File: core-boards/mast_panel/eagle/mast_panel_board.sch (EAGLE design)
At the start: 30 parts, among them J1 2-PIN_2MM-V, J4 4-PIN_2MM-H, U1 ATMEGA328P-AUR, U3 MCP2551T-I/SN

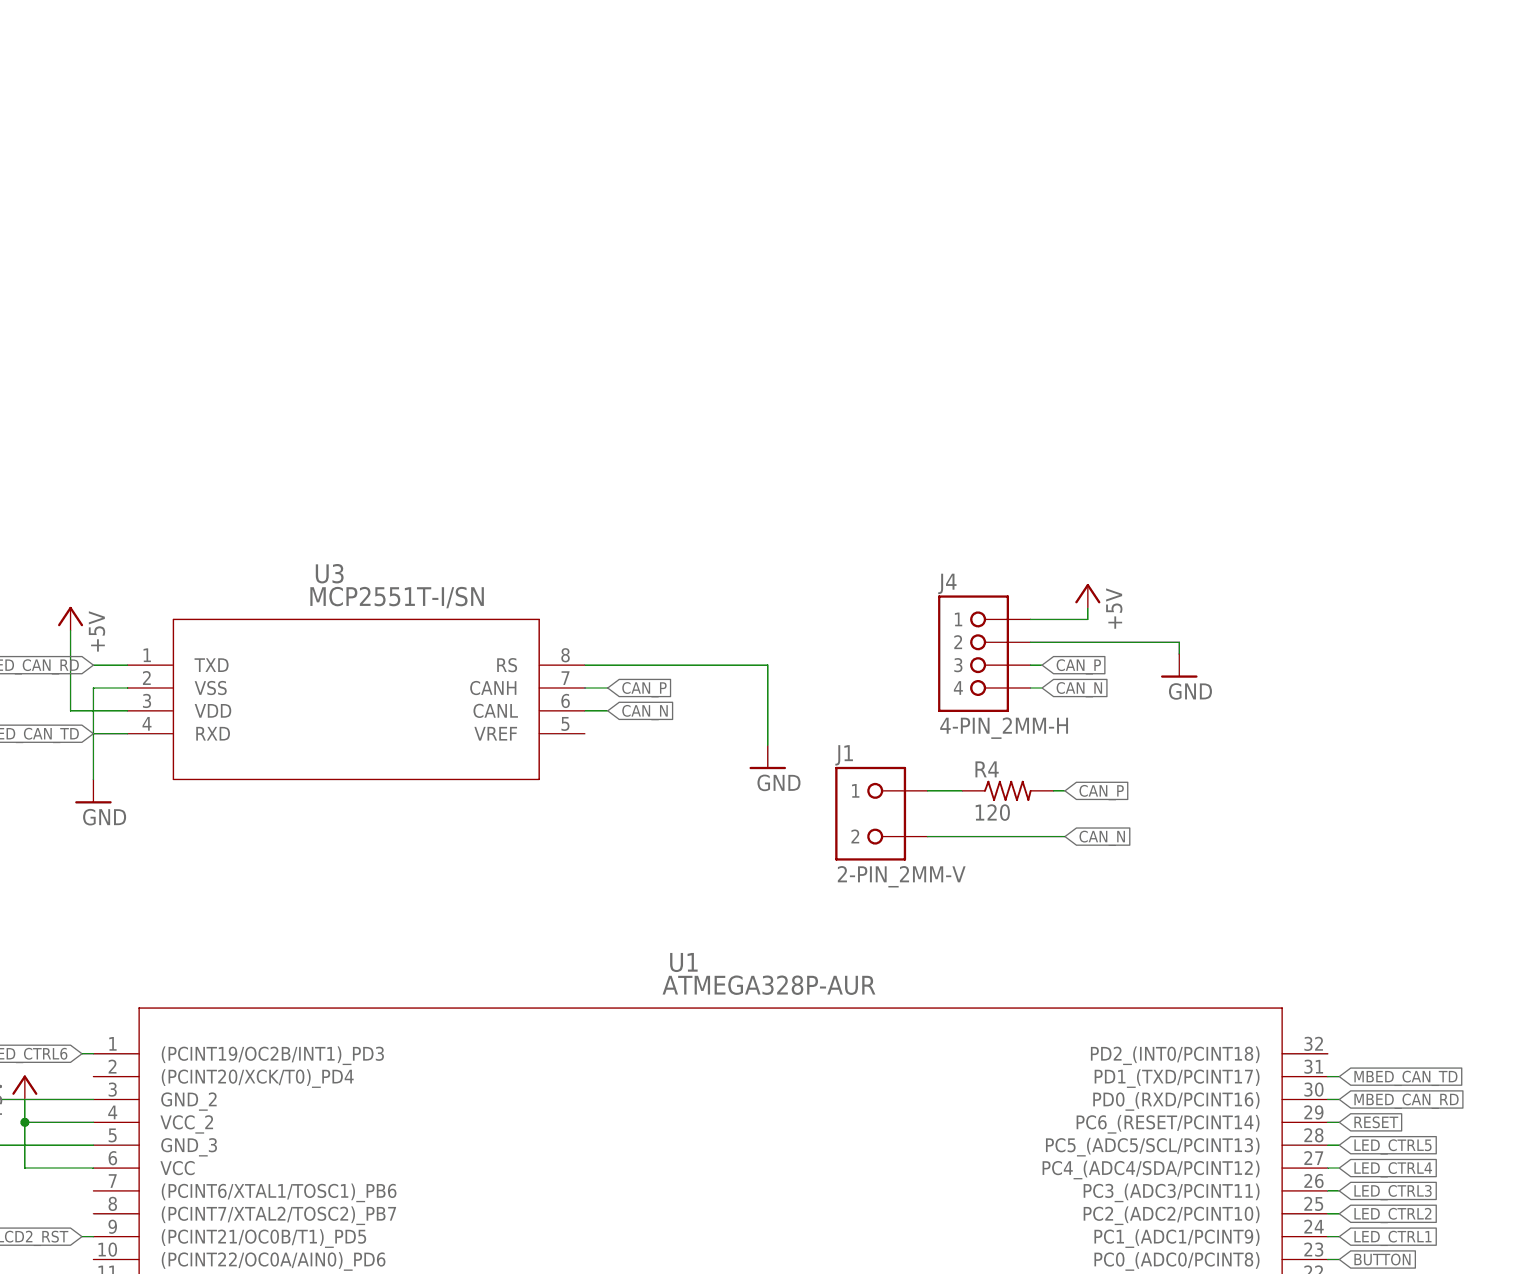
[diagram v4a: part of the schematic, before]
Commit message: CAN Addition
Added the new CAN Controller. Routing on the board still needs to be done.
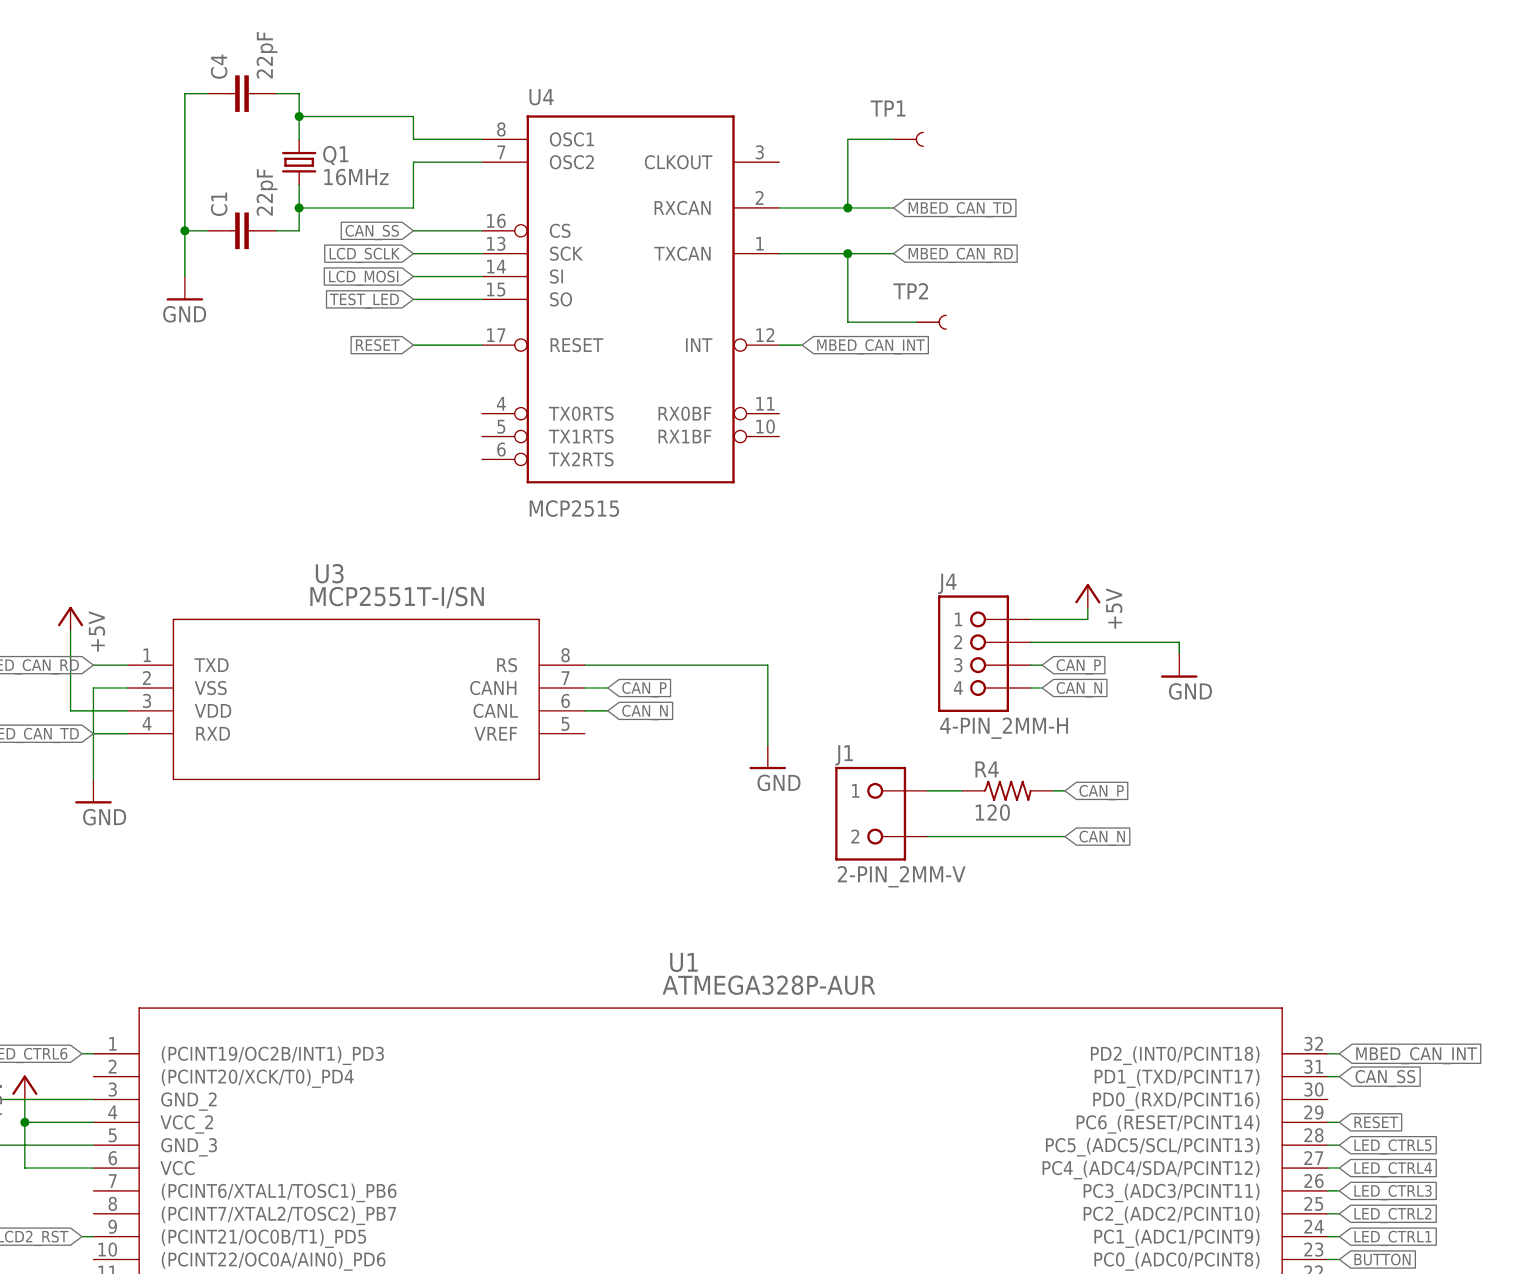
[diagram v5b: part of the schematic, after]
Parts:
- added C1, C4: 22pF, SparkFun-Capacitors:22PF-50V-5%(0603)
- added Q1: 16MHz, SparkFun-FreqCtrl:CRYSTAL5X3
- added TP1, TP2: TEST-POINT3X5, SparkFun-Passives:TEST-POINT3X5
- added U4: MCP2515, SparkFun-DigitalIC:MCP2510SO
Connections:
- new net CAN_SS: U1.PD1_(TXD/PCINT17), U4>NAME.CS
- new net MBED_CAN_INT: U1.PD2_(INT0/PCINT18), U4>NAME.INT
- new net N$17: C4.2, Q1.2, U4>NAME.OSC1
- new net N$18: C1.2, Q1.1, U4>NAME.OSC2
- net GND: now also C1.1, C4.1
- net LCD_MOSI: now also U4>NAME.SI
- net LCD_SCLK: now also U4>NAME.SCK
- net MBED_CAN_RD: now also TP2.1, U4>NAME.TXCAN; no longer U1.PD0_(RXD/PCINT16)
- net MBED_CAN_TD: now also TP1.1, U4>NAME.RXCAN; no longer U1.PD1_(TXD/PCINT17)
- net RESET: now also U4>NAME.RESET
- net TEST_LED: now also U4>NAME.SO
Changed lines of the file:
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@@
 <part name="R9" library="rcl" library_urn="urn:adsk.eagle:library:334" deviceset="R-US_" device="R0805" package3d_urn="urn:adsk.eagle:package:23553/2" value="50kO"/>
 <part name="R10" library="rcl" library_urn="urn:adsk.eagle:library:334" deviceset="R-US_" device="R0805" package3d_urn="urn:adsk.eagle:package:23553/2" value="50kO"/>
+<part name="U4" library="SparkFun-DigitalIC" deviceset="MCP2510" device="SO" value="MCP2515"/>
+<part name="Q1" library="SparkFun-FreqCtrl" deviceset="CRYSTAL" device="5X3" value="16MHz"/>
+<part name="C1" library="SparkFun-Capacitors" deviceset="22PF-50V-5%(0603)" device="" value="22pF"/>
+<part name="C4" library="SparkFun-Capacitors" deviceset="22PF-50V-5%(0603)" device="" value="22pF"/>
+<part name="GND14" library="SparkFun-Aesthetics" deviceset="GND" device=""/>
+<part name="TP1" library="SparkFun-Passives" deviceset="TEST-POINT" device="3X5" value="TEST-POINT3X5"/>
+<part name="TP2" library="SparkFun-Passives" deviceset="TEST-POINT" device="3X5" value="TEST-POINT3X5"/>
 </parts>
 <sheets>
@@
 <attribute name="VALUE" x="-44.45" y="-106.172" size="1.778" layer="96"/>
 </instance>
+<instance part="U4" gate="&gt;NAME" x="78.74" y="88.9" smashed="yes">
+<attribute name="NAME" x="68.58" y="105.41" size="1.778" layer="95"/>
+<attribute name="VALUE" x="68.58" y="59.69" size="1.778" layer="96"/>
+</instance>
+<instance part="Q1" gate="G$1" x="43.18" y="99.06" smashed="yes" rot="R90">
+<attribute name="NAME" x="45.72" y="99.06" size="1.778" layer="95"/>
+<attribute name="VALUE" x="45.72" y="96.52" size="1.778" layer="96"/>
+</instance>
+<instance part="C1" gate="G$1" x="38.1" y="91.44" smashed="yes" rot="R90">
+<attribute name="NAME" x="35.179" y="92.964" size="1.778" layer="95" rot="R90"/>
+<attribute name="VALUE" x="40.259" y="92.964" size="1.778" layer="96" rot="R90"/>
+</instance>
+<instance part="C4" gate="G$1" x="38.1" y="106.68" smashed="yes" rot="R90">
+<attribute name="NAME" x="35.179" y="108.204" size="1.778" layer="95" rot="R90"/>
+<attribute name="VALUE" x="40.259" y="108.204" size="1.778" layer="96" rot="R90"/>
+</instance>
+<instance part="GND14" gate="1" x="30.48" y="83.82" smashed="yes">
+<attribute name="VALUE" x="27.94" y="81.28" size="1.778" layer="96"/>
+</instance>
+<instance part="TP1" gate="G$1" x="109.22" y="101.6" smashed="yes">
+<attribute name="NAME" x="106.68" y="104.14" size="1.778" layer="95"/>
+</instance>
+<instance part="TP2" gate="G$1" x="111.76" y="81.28" smashed="yes">
+<attribute name="NAME" x="109.22" y="83.82" size="1.778" layer="95"/>
+</instance>
 </instances>
 <busses>
@@
 <pinref part="GND13" gate="1" pin="GND"/>
 </segment>
+<segment>
+<wire x1="33.02" y1="106.68" x2="30.48" y2="106.68" width="0.1524" layer="91"/>
+<wire x1="30.48" y1="106.68" x2="30.48" y2="91.44" width="0.1524" layer="91"/>
+<wire x1="30.48" y1="91.44" x2="33.02" y2="91.44" width="0.1524" layer="91"/>
+<wire x1="30.48" y1="86.36" x2="30.48" y2="91.44" width="0.1524" layer="91"/>
+<junction x="30.48" y="91.44"/>
+<pinref part="C4" gate="G$1" pin="1"/>
+<pinref part="C1" gate="G$1" pin="1"/>
+<pinref part="GND14" gate="1" pin="GND"/>
+</segment>
 </net>
 <net name="BUTTON" class="0">
@@
 </segment>
 <segment>
-<pinref part="U1" gate="A" pin="PD0_(RXD/PCINT16)"/>
-<wire x1="157.48" y1="-5.08" x2="158.75" y2="-5.08" width="0.1524" layer="91"/>
-<label x="158.75" y="-5.08" size="1.27" layer="95" xref="yes"/>
+<wire x1="96.52" y1="88.9" x2="104.14" y2="88.9" width="0.1524" layer="91"/>
+<pinref part="U4" gate="&gt;NAME" pin="TXCAN"/>
+<label x="109.22" y="88.9" size="1.27" layer="95" xref="yes"/>
+<pinref part="TP2" gate="G$1" pin="1"/>
+<wire x1="104.14" y1="88.9" x2="109.22" y2="88.9" width="0.1524" layer="91"/>
+<wire x1="111.76" y1="81.28" x2="104.14" y2="81.28" width="0.1524" layer="91"/>
+<wire x1="104.14" y1="81.28" x2="104.14" y2="88.9" width="0.1524" layer="91"/>
+<junction x="104.14" y="88.9"/>
 </segment>
 </net>
@@
 </segment>
 <segment>
-<pinref part="U1" gate="A" pin="PD1_(TXD/PCINT17)"/>
-<wire x1="157.48" y1="-2.54" x2="158.75" y2="-2.54" width="0.1524" layer="91"/>
-<label x="158.75" y="-2.54" size="1.27" layer="95" xref="yes"/>
+<wire x1="96.52" y1="93.98" x2="104.14" y2="93.98" width="0.1524" layer="91"/>
+<pinref part="U4" gate="&gt;NAME" pin="RXCAN"/>
+<label x="109.22" y="93.98" size="1.27" layer="95" xref="yes"/>
+<pinref part="TP1" gate="G$1" pin="1"/>
+<wire x1="104.14" y1="93.98" x2="109.22" y2="93.98" width="0.1524" layer="91"/>
+<wire x1="109.22" y1="101.6" x2="104.14" y2="101.6" width="0.1524" layer="91"/>
+<wire x1="104.14" y1="101.6" x2="104.14" y2="93.98" width="0.1524" layer="91"/>
+<junction x="104.14" y="93.98"/>
 </segment>
 </net>
@@
 <pinref part="JP2" gate="A" pin="6"/>
 </segment>
+<segment>
+<wire x1="63.5" y1="88.9" x2="55.88" y2="88.9" width="0.1524" layer="91"/>
+<pinref part="U4" gate="&gt;NAME" pin="SCK"/>
+<label x="55.88" y="88.9" size="1.27" layer="95" rot="R180" xref="yes"/>
+</segment>
 </net>
 <net name="LCD_MOSI" class="0">
@@
 <pinref part="JP2" gate="A" pin="5"/>
 </segment>
+<segment>
+<wire x1="63.5" y1="86.36" x2="55.88" y2="86.36" width="0.1524" layer="91"/>
+<pinref part="U4" gate="&gt;NAME" pin="SI"/>
+<label x="55.88" y="86.36" size="1.27" layer="95" rot="R180" xref="yes"/>
+</segment>
 </net>
 <net name="LCD1_SS" class="0">
@@
 <wire x1="26.67" y1="-128.27" x2="21.59" y2="-128.27" width="0.1524" layer="91"/>
 <label x="21.59" y="-128.27" size="1.27" layer="95" rot="R180" xref="yes"/>
+</segment>
+<segment>
+<wire x1="63.5" y1="83.82" x2="55.88" y2="83.82" width="0.1524" layer="91"/>
+<pinref part="U4" gate="&gt;NAME" pin="SO"/>
+<label x="55.88" y="83.82" size="1.27" layer="95" rot="R180" xref="yes"/>
 </segment>
 </net>
@@
 <pinref part="R3" gate="G$1" pin="1"/>
 </segment>
-</net>
+<segment>
+<wire x1="63.5" y1="78.74" x2="55.88" y2="78.74" width="0.1524" layer="91"/>
+<pinref part="U4" gate="&gt;NAME" pin="RESET"/>
+<label x="55.88" y="78.74" size="1.27" layer="95" rot="R180" xref="yes"/>
+</segment>
+</net>
+<net name="N$17" class="0">
+<segment>
+<wire x1="43.18" y1="101.6" x2="43.18" y2="104.14" width="0.1524" layer="91"/>
+<wire x1="43.18" y1="104.14" x2="43.18" y2="106.68" width="0.1524" layer="91"/>
+<wire x1="40.64" y1="106.68" x2="43.18" y2="106.68" width="0.1524" layer="91"/>
+<wire x1="63.5" y1="101.6" x2="55.88" y2="101.6" width="0.1524" layer="91"/>
+<wire x1="55.88" y1="101.6" x2="55.88" y2="104.14" width="0.1524" layer="91"/>
+<wire x1="55.88" y1="104.14" x2="43.18" y2="104.14" width="0.1524" layer="91"/>
+<junction x="43.18" y="104.14"/>
+<pinref part="Q1" gate="G$1" pin="2"/>
+<pinref part="C4" gate="G$1" pin="2"/>
+<pinref part="U4" gate="&gt;NAME" pin="OSC1"/>
+</segment>
+</net>
+<net name="N$18" class="0">
+<segment>
+<wire x1="43.18" y1="96.52" x2="43.18" y2="93.98" width="0.1524" layer="91"/>
+<wire x1="43.18" y1="93.98" x2="43.18" y2="91.44" width="0.1524" layer="91"/>
+<wire x1="40.64" y1="91.44" x2="43.18" y2="91.44" width="0.1524" layer="91"/>
+<wire x1="63.5" y1="99.06" x2="55.88" y2="99.06" width="0.1524" layer="91"/>
+<wire x1="55.88" y1="99.06" x2="55.88" y2="93.98" width="0.1524" layer="91"/>
+<wire x1="55.88" y1="93.98" x2="43.18" y2="93.98" width="0.1524" layer="91"/>
+<junction x="43.18" y="93.98"/>
+<pinref part="Q1" gate="G$1" pin="1"/>
+<pinref part="C1" gate="G$1" pin="2"/>
+<pinref part="U4" gate="&gt;NAME" pin="OSC2"/>
+</segment>
+</net>
+<net name="CAN_SS" class="0">
+<segment>
+<wire x1="63.5" y1="91.44" x2="55.88" y2="91.44" width="0.1524" layer="91"/>
+<pinref part="U4" gate="&gt;NAME" pin="CS"/>
+<label x="55.88" y="91.44" size="1.27" layer="95" rot="R180" xref="yes"/>
+</segment>
+<segment>
+<pinref part="U1" gate="A" pin="PD1_(TXD/PCINT17)"/>
+<wire x1="157.48" y1="-2.54" x2="158.75" y2="-2.54" width="0.1524" layer="91"/>
+<label x="158.75" y="-2.54" size="1.4224" layer="95" xref="yes"/>
+</segment>
+</net>
+<net name="MBED_CAN_INT" class="0">
+<segment>
+<wire x1="96.52" y1="78.74" x2="99.06" y2="78.74" width="0.1524" layer="91"/>
+<pinref part="U4" gate="&gt;NAME" pin="INT"/>
+<label x="99.06" y="78.74" size="1.27" layer="95" xref="yes"/>
+</segment>
+<segment>
+<pinref part="U1" gate="A" pin="PD2_(INT0/PCINT18)"/>
+<wire x1="157.48" y1="0" x2="158.75" y2="0" width="0.1524" layer="91"/>
+<label x="158.75" y="0" size="1.4224" layer="95" xref="yes"/>
+</segment>
+</net>
